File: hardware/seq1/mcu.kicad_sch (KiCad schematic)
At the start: 16 parts, among them J6 Conn_02x06_Odd_Even, SW10 SW_Push, SW11 SW_Push, SW9 PEC12R-3220F-S0024, U5 128x64 0.96" OLED I2C

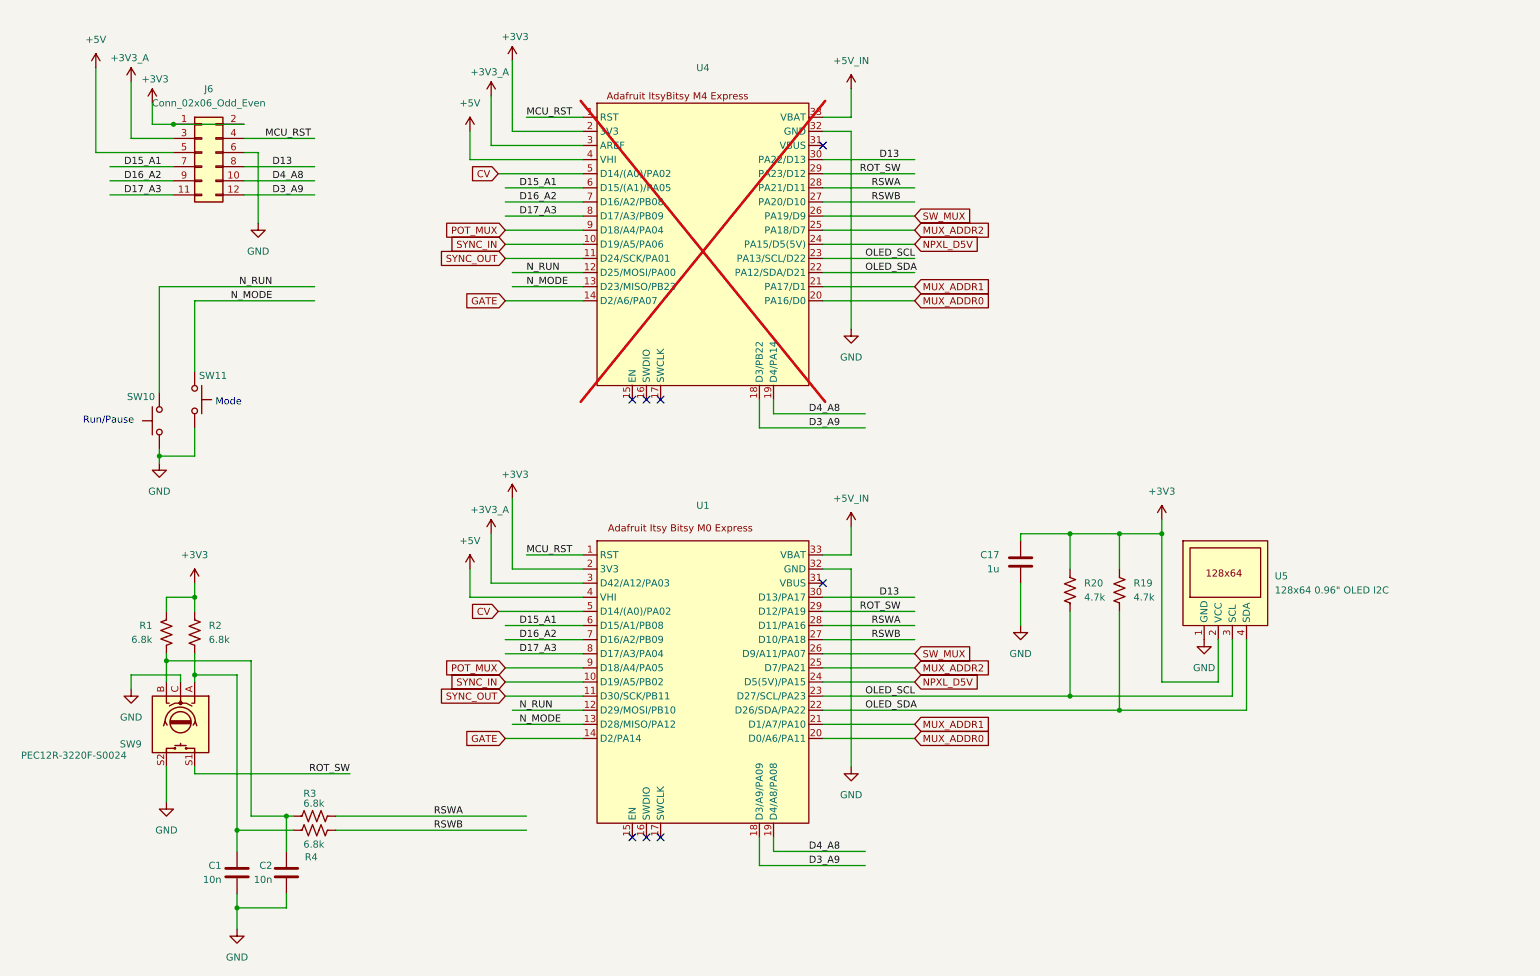
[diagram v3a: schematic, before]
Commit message: updating the board with new line in
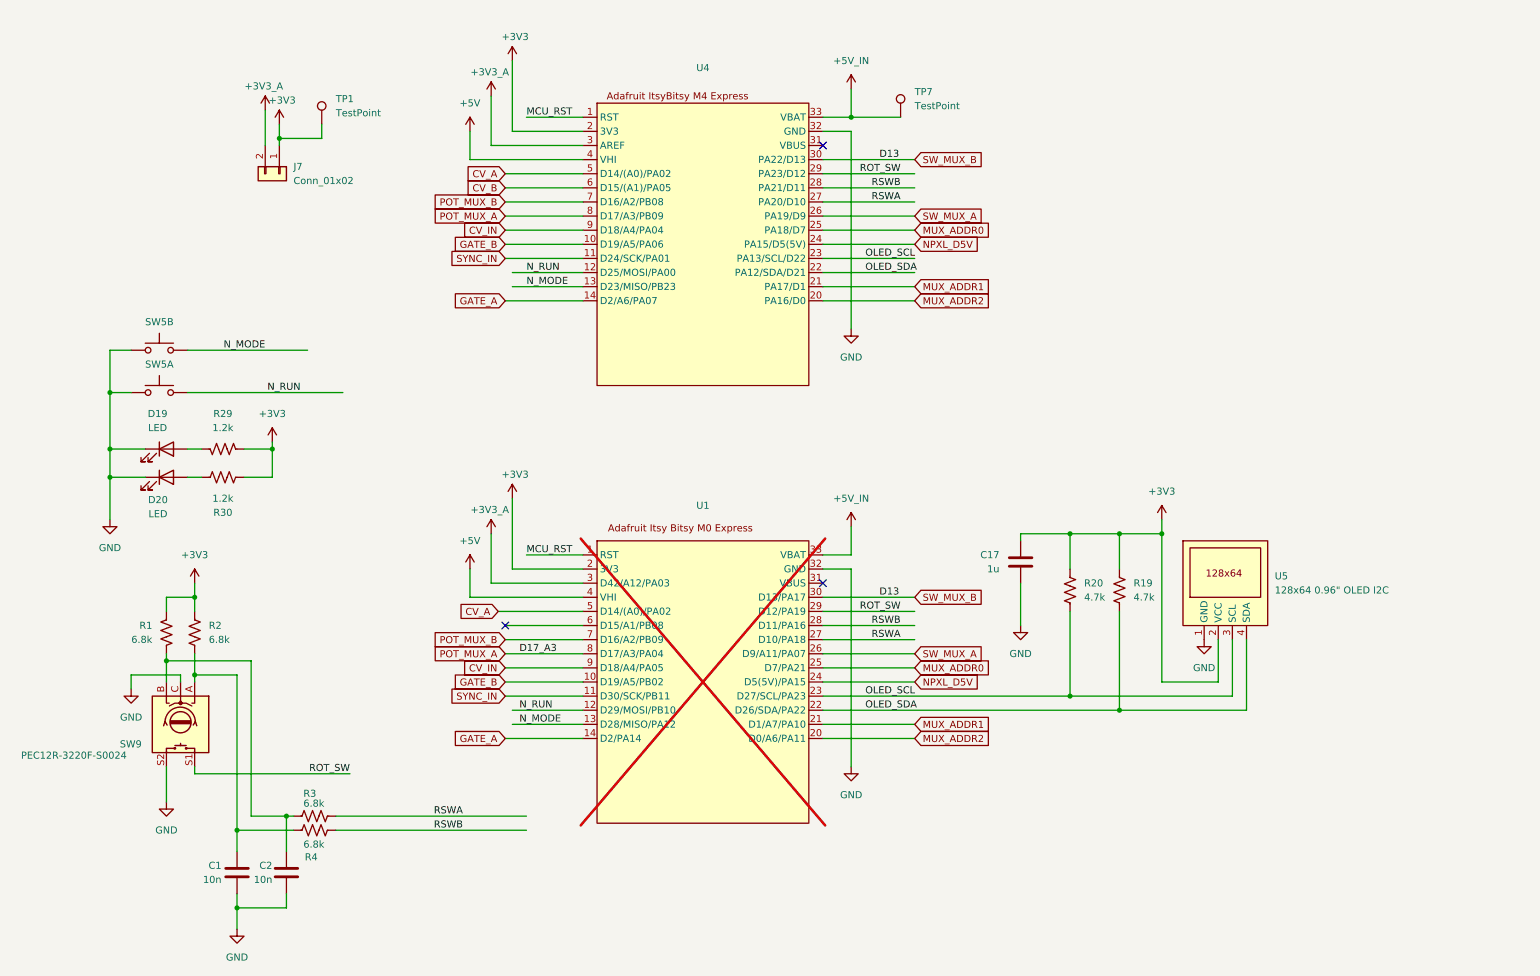
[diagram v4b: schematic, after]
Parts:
- removed J6: Conn_02x06_Odd_Even, Connector_PinHeader_2.54mm:PinHeader_2x06_P2.54mm_Vertical, symbol Connector_Generic:Conn_02x06_Odd_Even
- removed SW10, SW11: SW_Push, Button_Switch_THT:SW_PUSH_6mm_H5mm, symbol Switch:SW_Push
- removed U1: ~, Module_Custom:Adafruit_ItsyBitsy_M0_Express, symbol MCU_Module_Custom:Adafruit_ItsyBitsy_M0_Express
- removed U4: ~, symbol MCU_Module_Custom:Adafruit_ItsyBitsy_M4_Express
- added D19, D20: LED, Adafruit_Trellis:LED_3mm_Backside_SMD, symbol Device:LED
- added J7: Conn_01x02, Connector_PinHeader_2.54mm:PinHeader_1x02_P2.54mm_Vertical, symbol Connector_Generic:Conn_01x02
- added R29, R30: 1.2k, Resistor_THT:R_Axial_DIN0204_L3.6mm_D1.6mm_P2.54mm_Vertical, symbol Device:R_US
- added SW5: SW_Push_x2, Adafruit_Trellis:SW_Silicone_Keypad_PushButton_10mm_2x1grid_NH, symbol Adafruit_Trellis:SW_Push_x2
- added TP1, TP7: TestPoint, Connector_PinHeader_2.54mm:PinHeader_1x01_P2.54mm_Vertical, symbol Connector:TestPoint
- added U1: ~, Module_Custom:Adafruit_ItsyBitsy_M0_Express_DIP, symbol MCU_Module_Custom:Adafruit_ItsyBitsy_M0_Express_DIP
- added U4: ~, Module_Custom:Adafruit_ItsyBitsy_M0_Express_DIP, symbol MCU_Module_Custom:Adafruit_ItsyBitsy_M4_Express_DIP
- C1, C17, C2: footprint Capacitor_THT:C_Disc_D5.0mm_W2.5mm_P5.00mm -> Capacitor_THT:C_Disc_D5.0mm_W2.5mm_P2.50mm
- R1, R2, R3, R4: footprint Resistor_THT:R_Axial_DIN0207_L6.3mm_D2.5mm_P2.54mm_Vertical -> Resistor_THT:R_Axial_DIN0204_L3.6mm_D1.6mm_P2.54mm_Vertical
- R19, R20: footprint Resistor_THT:R_Axial_DIN0207_L6.3mm_D2.5mm_P10.16mm_Horizontal -> Resistor_THT:R_Axial_DIN0204_L3.6mm_D1.6mm_P2.54mm_Vertical
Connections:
- net +3V3: now also J7.1 (Pin_1), R29.2, R30.2, TP1.1, U1.2 (3V3), U4.2 (3V3)
- net +3V3_A: now also J7.2 (Pin_2), U1.3 (D42/A12/PA03), U4.3 (AREF)
- net +5V: now also U1.4 (VHI), U4.4 (VHI)
- net +5V_IN: now also TP7.1, U1.33 (VBAT), U4.33 (VBAT)
- net GND: now also D19.1 (K), D20.1 (K), SW5.2, SW5.4, U1.32 (GND), U4.32 (GND)
- net MCU_RST: now also U1.1 (RST), U4.1 (RST)
- net MUX_ADDR0: now also U1.25 (D7/PA21), U4.25 (PA18/D7)
- net MUX_ADDR1: now also U1.21 (D1/A7/PA10), U4.21 (PA17/D1)
- net MUX_ADDR2: now also U1.20 (D0/A6/PA11), U4.20 (PA16/D0)
- net NPXL_D5V: now also U1.24 (D5(5V)/PA15), U4.24 (PA15/D5(5V))
- net N_MODE: now also SW5.3, U1.13 (D28/MISO/PA12), U4.13 (D23/MISO/PB23)
- net N_RUN: now also SW5.1, U1.12 (D29/MOSI/PB10), U4.12 (D25/MOSI/PA00)
- net OLED_SCL: now also U1.23 (D27/SCL/PA23), U4.23 (PA13/SCL/D22)
- net OLED_SDA: now also U1.22 (D26/SDA/PA22), U4.22 (PA12/SDA/D21)
- net ROT_SW: now also U1.29 (D12/PA19), U4.29 (PA23/D12)
- net RSWA: now also U1.27 (D10/PA18), U4.27 (PA20/D10)
- net RSWB: now also U1.28 (D11/PA16), U4.28 (PA21/D11)
- net SYNC_IN: now also U1.11 (D30/SCK/PB11), U4.11 (D24/SCK/PA01)
- new net: D20.2 (A), R30.1
- new net: D19.2 (A), R29.1
- new net CV_A: U1.5 (D14/(A0)/PA02), U4.5 (D14/(A0)/PA02)
- new net CV_B: U4.6 (D15/(A1)/PA05)
- new net CV_IN: U1.9 (D18/A4/PA05), U4.9 (D18/A4/PA04)
- new net GATE_A: U1.14 (D2/PA14), U4.14 (D2/A6/PA07)
- new net GATE_B: U1.10 (D19/A5/PB02), U4.10 (D19/A5/PA06)
- new net POT_MUX_A: U1.8 (D17/A3/PA04), U4.8 (D17/A3/PB09)
- new net POT_MUX_B: U1.7 (D16/A2/PB09), U4.7 (D16/A2/PB08)
- new net SW_MUX_A: U1.26 (D9/A11/PA07), U4.26 (PA19/D9)
- new net SW_MUX_B: U1.30 (D13/PA17), U4.30 (PA22/D13)
- no-connect marks 8 -> 3
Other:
- note removed: "Mode"
- note removed: "Run/Pause"
- company: (none) -> idyllm
- title: (none) -> Sequencer

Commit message: layout for v2 board (WIP) with risers part of same schematic/PBC
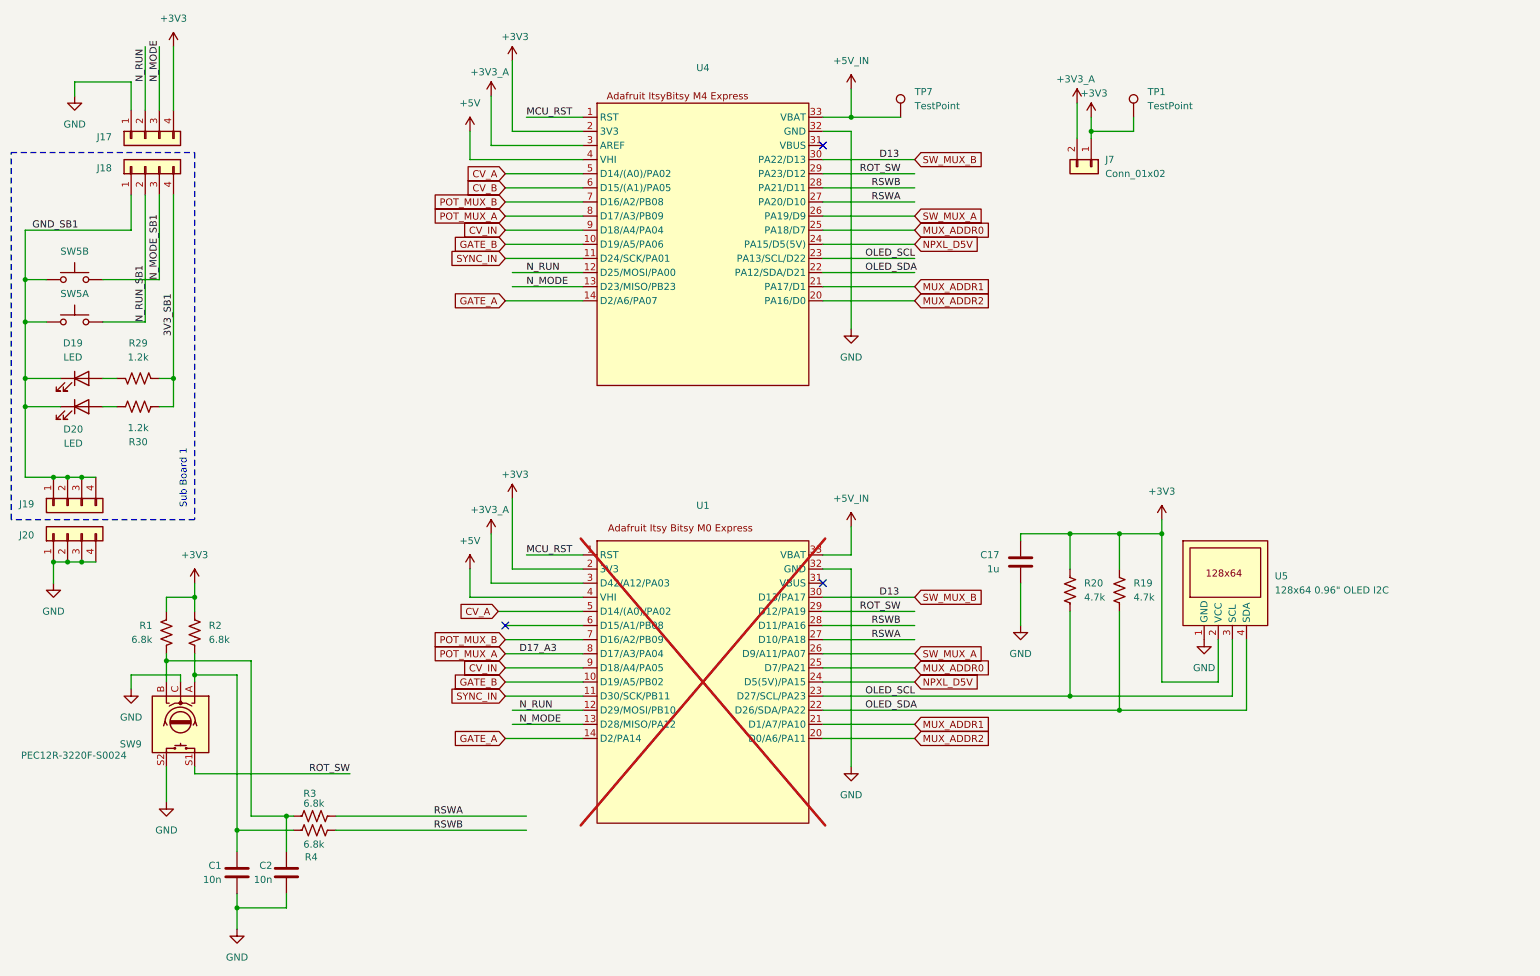
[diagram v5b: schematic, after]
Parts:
- added J17, J18, J19, J20: Conn_01x04, Connector_PinHeader_2.54mm:PinHeader_1x04_P2.54mm_Vertical, symbol Connector_Generic:Conn_01x04
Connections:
- net +3V3: now also J17.4 (Pin_4); no longer R29.2, R30.2
- net GND: now also J17.1 (Pin_1), J20.1 (Pin_1), J20.2 (Pin_2), J20.3 (Pin_3), J20.4 (Pin_4); no longer D19.1 (K), D20.1 (K), SW5.2, SW5.4
- net N_MODE: now also J17.3 (Pin_3); no longer SW5.3
- net N_RUN: now also J17.2 (Pin_2); no longer SW5.1
- new net 3V3_SB1: J18.4 (Pin_4), R29.2, R30.2
- new net GND_SB1: D19.1 (K), D20.1 (K), J18.1 (Pin_1), J19.1 (Pin_1), J19.2 (Pin_2), J19.3 (Pin_3), J19.4 (Pin_4), SW5.2, SW5.4
- new net N_MODE_SB1: J18.3 (Pin_3), SW5.3
- new net N_RUN_SB1: J18.2 (Pin_2), SW5.1
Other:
- note added: "Sub Board 1"
- moved on the sheet: D19, D20, J7, R29, R30, SW5A, SW5B, TP1

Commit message: updated schematic title blocks for v2, generated gerbers
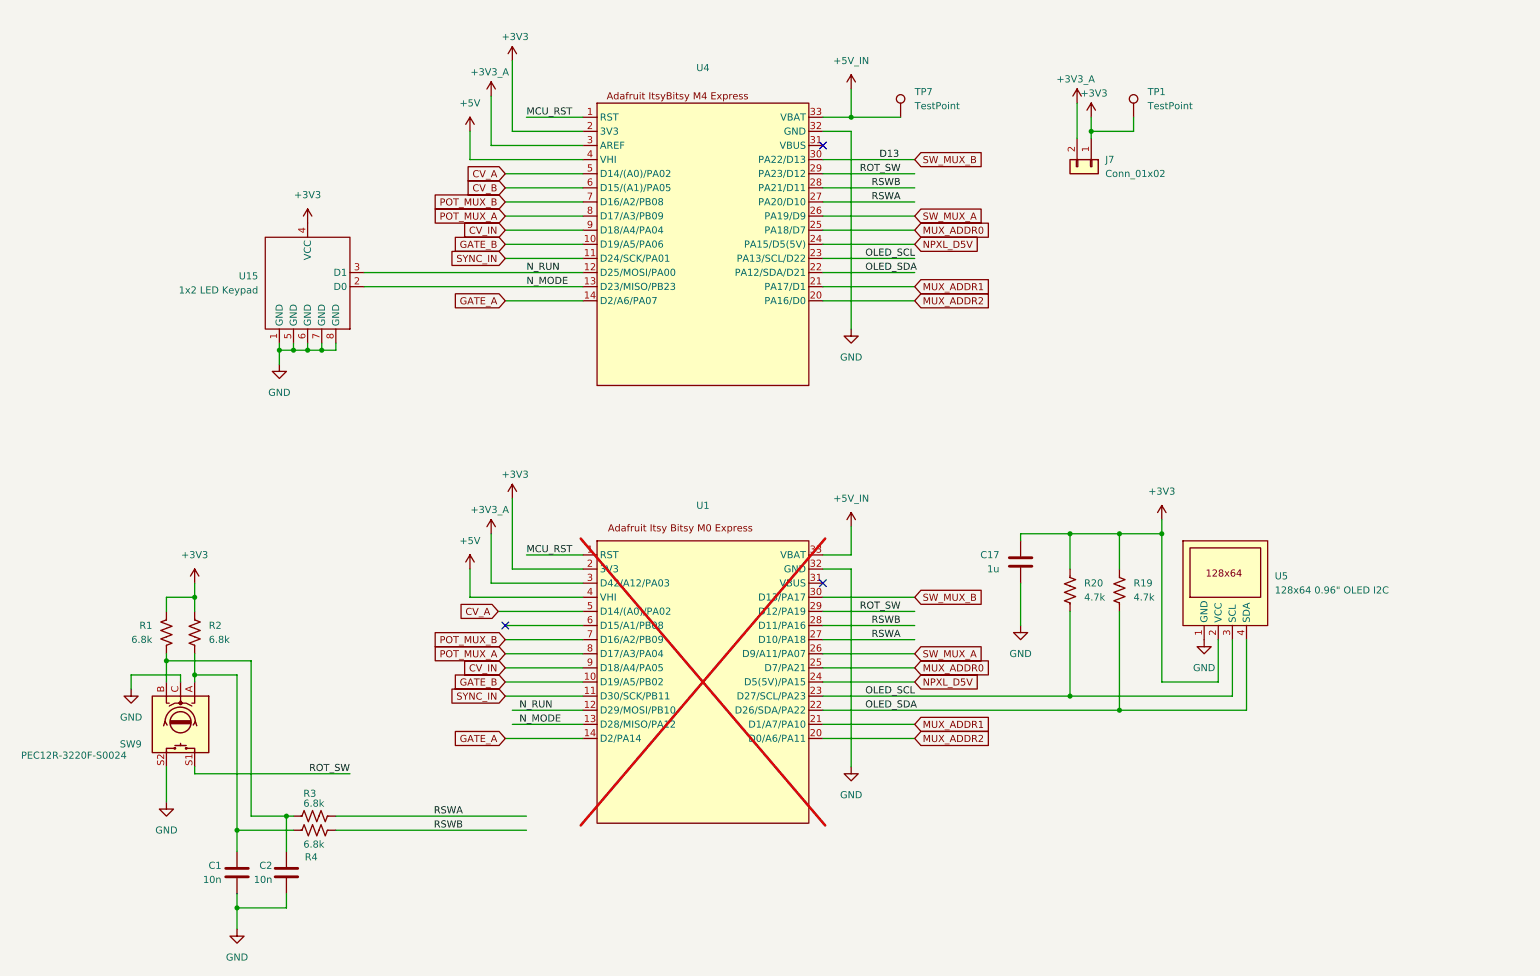
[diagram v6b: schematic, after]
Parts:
- removed D19, D20: LED, Adafruit_Trellis:LED_3mm_Backside_SMD, symbol Device:LED
- removed J17, J18, J19, J20: Conn_01x04, Connector_PinHeader_2.54mm:PinHeader_1x04_P2.54mm_Vertical, symbol Connector_Generic:Conn_01x04
- removed R29, R30: 1.2k, Resistor_THT:R_Axial_DIN0204_L3.6mm_D1.6mm_P2.54mm_Vertical, symbol Device:R_US
- removed SW5: SW_Push_x2, Adafruit_Trellis:SW_Silicone_Keypad_PushButton_10mm_2x1grid_NH, symbol Adafruit_Trellis:SW_Push_x2
- added U15: 1x2 LED Keypad, Adafruit_Trellis:SW_Keypad_PushButton_1x2_Riser, symbol Adafruit_Trellis:SW_LED_Keypad_1x2_Riser
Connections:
- net +3V3: now also U15.4 (VCC)
- net GND: now also U15.1 (GND), U15.5 (GND), U15.6 (GND), U15.7 (GND), U15.8 (GND)
- net N_MODE: now also U15.2 (D0)
- net N_RUN: now also U15.3 (D1)
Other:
- note removed: "Sub Board 1"
